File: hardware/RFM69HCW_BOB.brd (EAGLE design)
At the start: 27.9 x 20.3 mm, 13 parts, among them U1 RFM69HCW

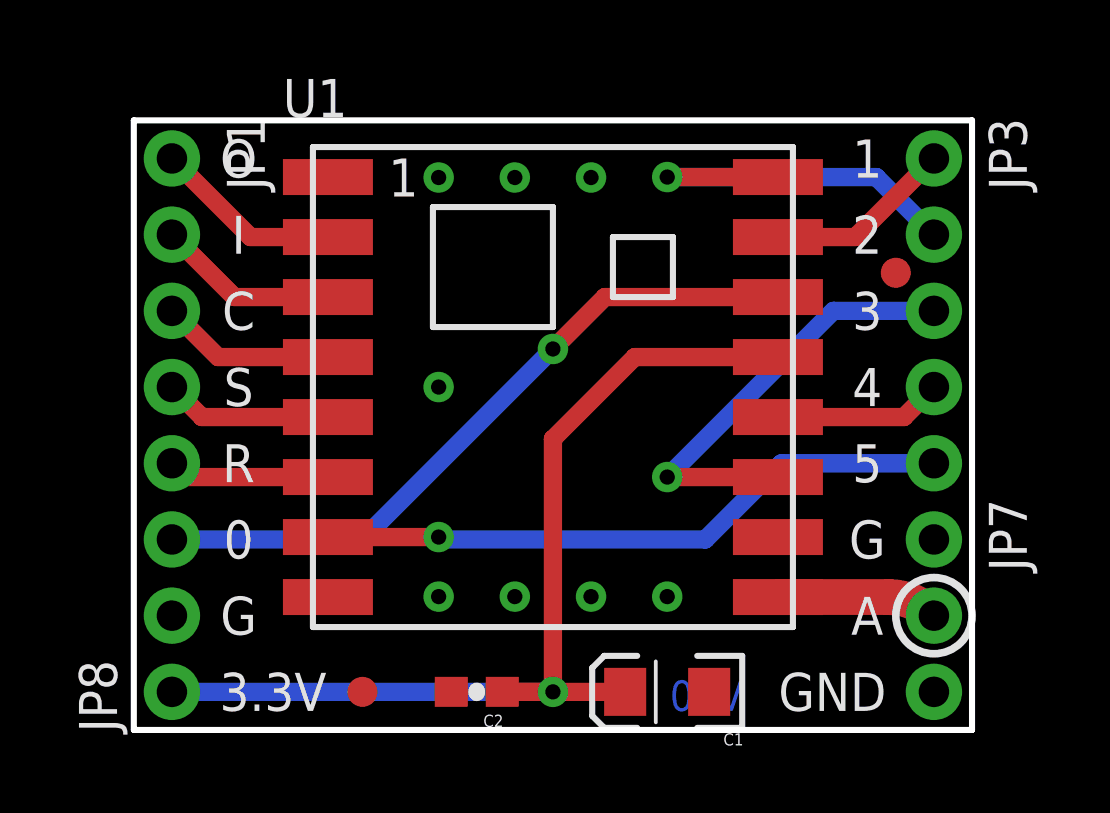
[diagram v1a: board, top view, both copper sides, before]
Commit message: Changed capacitor, removed C variant
Changed C1 to CAP-9824 (10uF ceramic for better transient response)
Removed RFM69C (low power) for future BOB
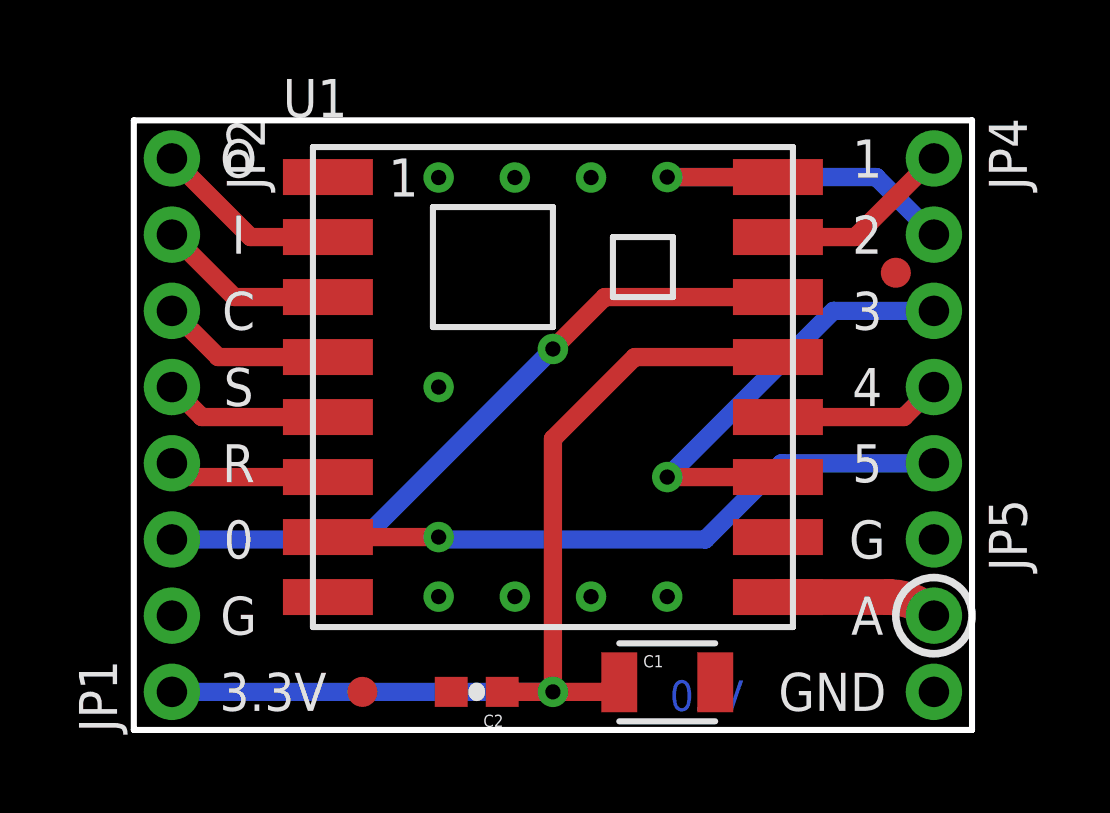
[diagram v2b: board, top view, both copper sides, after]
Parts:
- removed JP8: (no value), mike-temp:1X02_NO_SILK
- added JP4: (no value), mike-temp:1X05_ROUNDONLY_NOSILK
- C1: device SparkFun-Capacitors:EIA3216 -> SparkFun-Capacitors:1210
- JP1: device mike-temp:1X05_ROUNDONLY_NOSILK -> mike-temp:1X02_NO_SILK
- JP2: device mike-temp:1X01NS -> mike-temp:1X05_ROUNDONLY_NOSILK
- JP3: device mike-temp:1X05_ROUNDONLY_NOSILK -> mike-temp:1X01NS
- moved JP3 28.4 mm to (1.27, 6.35), turned to 0 degrees
- moved JP1 17.8 mm to (1.27, 1.27), turned to 90 degrees
- moved JP2 12.7 mm to (1.27, 19.1), turned to 270 degrees
- moved C1 0.32 mm to (17.8, 1.59), turned to 0 degrees
- renumbered JP7 to JP5
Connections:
- net 3.3V: now also C1.1, JP1.1; no longer C1.A, JP8.1
- net DIO0: now also JP3.1; no longer JP2.1
- net DIO1: now also JP4.1; no longer JP3.1
- net DIO2: now also JP4.2; no longer JP3.2
- net DIO3: now also JP4.3; no longer JP3.3
- net DIO4: now also JP4.4; no longer JP3.4
- net DIO5: now also JP4.5; no longer JP3.5
- net GND: now also C1.2, JP1.2; no longer C1.C, JP8.2
- net MISO: now also JP2.1; no longer JP1.1
- net MOSI: now also JP2.2; no longer JP1.2
- net NSS: now also JP2.4; no longer JP1.4
- net RESET: now also JP2.5; no longer JP1.5
- net SCK: now also JP2.3; no longer JP1.3
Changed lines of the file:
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@@
 <grid distance="0.05" unitdist="inch" unit="inch" style="lines" multiple="2" display="yes" altdistance="0.0125" altunitdist="inch" altunit="inch"/>
 <layers>
-<layer number="1" name="Top" color="4" fill="1" visible="yes" active="yes"/>
+<layer number="1" name="Top" color="4" fill="1" visible="no" active="yes"/>
 <layer number="2" name="Route2" color="1" fill="3" visible="no" active="no"/>
 <layer number="3" name="Route3" color="4" fill="3" visible="no" active="no"/>
@@
 <layer number="19" name="Unrouted" color="6" fill="1" visible="yes" active="yes"/>
 <layer number="20" name="Dimension" color="15" fill="1" visible="yes" active="yes"/>
-<layer number="21" name="tPlace" color="7" fill="1" visible="yes" active="yes"/>
-<layer number="22" name="bPlace" color="7" fill="1" visible="no" active="yes"/>
-<layer number="23" name="tOrigins" color="15" fill="1" visible="yes" active="yes"/>
-<layer number="24" name="bOrigins" color="15" fill="1" visible="no" active="yes"/>
+<layer number="21" name="tPlace" color="7" fill="1" visible="no" active="yes"/>
+<layer number="22" name="bPlace" color="7" fill="1" visible="yes" active="yes"/>
+<layer number="23" name="tOrigins" color="15" fill="1" visible="no" active="yes"/>
+<layer number="24" name="bOrigins" color="15" fill="1" visible="yes" active="yes"/>
 <layer number="25" name="tNames" color="7" fill="1" visible="no" active="yes"/>
 <layer number="26" name="bNames" color="7" fill="1" visible="no" active="yes"/>
 <layer number="27" name="tValues" color="7" fill="1" visible="no" active="yes"/>
 <layer number="28" name="bValues" color="7" fill="1" visible="no" active="yes"/>
-<layer number="29" name="tStop" color="7" fill="3" visible="yes" active="yes"/>
-<layer number="30" name="bStop" color="7" fill="6" visible="no" active="yes"/>
-<layer number="31" name="tCream" color="7" fill="4" visible="yes" active="yes"/>
+<layer number="29" name="tStop" color="7" fill="3" visible="no" active="yes"/>
+<layer number="30" name="bStop" color="7" fill="6" visible="yes" active="yes"/>
+<layer number="31" name="tCream" color="7" fill="4" visible="no" active="yes"/>
 <layer number="32" name="bCream" color="7" fill="5" visible="no" active="yes"/>
 <layer number="33" name="tFinish" color="6" fill="3" visible="no" active="yes"/>
@@
 <text x="19.05" y="2.54" size="1.27" layer="22" ratio="15" rot="MR0">(6.5" 164mm)</text>
 <text x="19.05" y="6.35" size="1.27" layer="22" ratio="15" rot="MR0">(3.1" 78mm)</text>
+<rectangle x1="19.05" y1="0.635" x2="20.32" y2="1.905" layer="22"/>
+<rectangle x1="11.43" y1="0.635" x2="12.7" y2="1.905" layer="22"/>
 </plain>
 <attributes>
@@
 <attribute name="PROD_ID" value="CAP-00810" x="-3.81" y="38.1" size="1.778" layer="27" rot="R180" display="off"/>
 </element>
-<element name="C1" library="SparkFun-Capacitors" package="EIA3216" value="10uF" x="17.78" y="1.27" rot="R180">
-<attribute name="PROD_ID" value="CAP-00811" x="-27.94" y="31.75" size="1.778" layer="27" rot="R180" display="off"/>
-</element>
 <element name="LOGO1" library="SparkFun-Aesthetics" package="SFE_LOGO_NAME_.1" value="SFE_LOGO_NAME.1_INCH" x="20.0025" y="14.2875" rot="MR0"/>
 <element name="LOGO2" library="SparkFun-Aesthetics" package="OSHW-LOGO-S" value="OSHW-LOGOS" x="13.97" y="11.43" rot="MR0"/>
-<element name="JP7" library="mike-temp" package="1X03_ROUND_ONLY_NO_SILK" value="ANTENNA" x="26.67" y="6.35" rot="R270"/>
-<element name="JP8" library="mike-temp" package="1X02_NO_SILK" value="" x="1.27" y="1.27" rot="R90"/>
-<element name="JP1" library="mike-temp" package="1X05_ROUNDONLY_NOSILK" value="" x="1.27" y="19.05" rot="R270"/>
-<element name="JP2" library="mike-temp" package="1X01NS" value="" x="1.27" y="6.35"/>
-<element name="JP3" library="mike-temp" package="1X05_ROUNDONLY_NOSILK" value="" x="26.67" y="19.05" rot="R270"/>
+<element name="JP5" library="mike-temp" package="1X03_ROUND_ONLY_NO_SILK" value="ANTENNA" x="26.67" y="6.35" rot="R270"/>
+<element name="JP1" library="mike-temp" package="1X02_NO_SILK" value="" x="1.27" y="1.27" rot="R90"/>
+<element name="JP2" library="mike-temp" package="1X05_ROUNDONLY_NOSILK" value="" x="1.27" y="19.05" rot="R270"/>
+<element name="JP3" library="mike-temp" package="1X01NS" value="" x="1.27" y="6.35"/>
+<element name="JP4" library="mike-temp" package="1X05_ROUNDONLY_NOSILK" value="" x="26.67" y="19.05" rot="R270"/>
 <element name="FID1" library="SparkFun-Aesthetics" package="FIDUCIAL-1X2" value="FIDUCIAL1X2" x="7.62" y="1.27"/>
 <element name="FID2" library="SparkFun-Aesthetics" package="FIDUCIAL-1X2" value="FIDUCIAL1X2" x="25.4" y="15.24"/>
+<element name="C1" library="SparkFun-Capacitors" package="1210" value="10uF" x="17.78" y="1.5875">
+<attribute name="PROD_ID" value="CAP-09824" x="17.78" y="1.5875" size="1.778" layer="27" display="off"/>
+</element>
 </elements>
 <signals>
@@
 <contactref element="U1" pad="8"/>
 <contactref element="U1" pad="1"/>
-<contactref element="C1" pad="C"/>
 <contactref element="C2" pad="2"/>
 <polygon width="0.2032" layer="16" isolate="0.3048">
@@
 <via x="17.78" y="4.445" extent="1-16" drill="0.508"/>
 <via x="10.16" y="4.445" extent="1-16" drill="0.508"/>
-<contactref element="JP7" pad="1"/>
-<contactref element="JP7" pad="3"/>
+<contactref element="JP5" pad="1"/>
+<contactref element="JP5" pad="3"/>
 <contactref element="U1" pad="10"/>
 <via x="12.7" y="4.445" extent="1-16" drill="0.508"/>
 <via x="15.24" y="4.445" extent="1-16" drill="0.508"/>
-<contactref element="JP8" pad="2"/>
+<contactref element="JP1" pad="2"/>
 <via x="12.7" y="18.415" extent="1-16" drill="0.508"/>
 <via x="15.24" y="18.415" extent="1-16" drill="0.508"/>
 <via x="10.16" y="18.415" extent="1-16" drill="0.508"/>
 <via x="10.16" y="11.43" extent="1-16" drill="0.508"/>
+<contactref element="C1" pad="2"/>
 </signal>
 <signal name="3.3V">
 <contactref element="C2" pad="1"/>
-<contactref element="C1" pad="A"/>
 <wire x1="16.699759375" y1="12.43" x2="13.97" y2="9.700240625" width="0.6096" layer="1"/>
 <wire x1="13.97" y1="9.700240625" x2="13.97" y2="1.27" width="0.6096" layer="1"/>
 <via x="13.97" y="1.27" extent="1-16" drill="0.508"/>
-<wire x1="13.97" y1="1.27" x2="16.38" y2="1.27" width="0.6096" layer="1"/>
 <wire x1="13.97" y1="1.27" x2="12.28" y2="1.27" width="0.6096" layer="1"/>
-<contactref element="JP8" pad="1"/>
+<contactref element="JP1" pad="1"/>
 <contactref element="U1" pad="13"/>
 <wire x1="16.699759375" y1="12.43" x2="21.47" y2="12.43" width="0.6096" layer="1"/>
 <wire x1="1.27" y1="1.27" x2="13.97" y2="1.27" width="0.6096" layer="16"/>
+<contactref element="C1" pad="1"/>
+<wire x1="13.97" y1="1.27" x2="16.18" y2="1.27" width="0.6096" layer="1"/>
+<wire x1="16.18" y1="1.27" x2="16.18" y2="1.5875" width="0.6096" layer="1"/>
 </signal>
 <signal name="DIO0">
 <contactref element="U1" pad="14"/>
-<contactref element="JP2" pad="1"/>
+<contactref element="JP3" pad="1"/>
 <wire x1="21.47" y1="14.43" x2="15.7" y2="14.43" width="0.6096" layer="1"/>
 <wire x1="15.7" y1="14.43" x2="13.97" y2="12.7" width="0.6096" layer="1"/>
@@
 <signal name="DIO1">
 <contactref element="U1" pad="15"/>
-<contactref element="JP3" pad="1"/>
+<contactref element="JP4" pad="1"/>
 <wire x1="21.47" y1="16.43" x2="24.05" y2="16.43" width="0.6096" layer="1"/>
 <wire x1="24.05" y1="16.43" x2="26.67" y2="19.05" width="0.6096" layer="1"/>
@@
 <signal name="DIO2">
 <contactref element="U1" pad="16"/>
-<contactref element="JP3" pad="2"/>
+<contactref element="JP4" pad="2"/>
 <wire x1="21.47" y1="18.43" x2="17.78" y2="18.43" width="0.6096" layer="1"/>
 <via x="17.78" y="18.43" extent="1-16" drill="0.508"/>
@@
 <signal name="DIO3">
 <contactref element="U1" pad="11"/>
-<contactref element="JP3" pad="3"/>
+<contactref element="JP4" pad="3"/>
 <wire x1="21.47" y1="8.43" x2="17.78" y2="8.43" width="0.6096" layer="1"/>
 <via x="17.78" y="8.43" extent="1-16" drill="0.508"/>
@@
 <contactref element="U1" pad="2"/>
 <wire x1="6.47" y1="16.43" x2="3.89" y2="16.43" width="0.6096" layer="1"/>
-<contactref element="JP1" pad="1"/>
+<contactref element="JP2" pad="1"/>
 <wire x1="3.89" y1="16.43" x2="1.27" y2="19.05" width="0.6096" layer="1"/>
 </signal>
@@
 <contactref element="U1" pad="3"/>
 <wire x1="6.47" y1="14.43" x2="3.35" y2="14.43" width="0.6096" layer="1"/>
-<contactref element="JP1" pad="2"/>
+<contactref element="JP2" pad="2"/>
 <wire x1="3.35" y1="14.43" x2="1.27" y2="16.51" width="0.6096" layer="1"/>
 </signal>
@@
 <contactref element="U1" pad="4"/>
 <wire x1="6.47" y1="12.43" x2="2.81" y2="12.43" width="0.6096" layer="1"/>
-<contactref element="JP1" pad="3"/>
+<contactref element="JP2" pad="3"/>
 <wire x1="2.81" y1="12.43" x2="1.27" y2="13.97" width="0.6096" layer="1"/>
 </signal>
@@
 <contactref element="U1" pad="5"/>
 <wire x1="6.47" y1="10.43" x2="2.27" y2="10.43" width="0.6096" layer="1"/>
-<contactref element="JP1" pad="4"/>
+<contactref element="JP2" pad="4"/>
 <wire x1="2.27" y1="10.43" x2="1.27" y2="11.43" width="0.6096" layer="1"/>
 </signal>
@@
 <contactref element="U1" pad="6"/>
 <wire x1="6.47" y1="8.43" x2="1.73" y2="8.43" width="0.6096" layer="1"/>
-<contactref element="JP1" pad="5"/>
+<contactref element="JP2" pad="5"/>
 <wire x1="1.73" y1="8.43" x2="1.27" y2="8.89" width="0.6096" layer="1"/>
 </signal>
 <signal name="ANT">
-<contactref element="JP7" pad="2"/>
+<contactref element="JP5" pad="2"/>
 <contactref element="U1" pad="9"/>
 <wire x1="21.47" y1="4.43" x2="25.1731875" y2="4.43" width="1.1938" layer="1"/>
@@
 <signal name="DIO5">
 <contactref element="U1" pad="7"/>
-<contactref element="JP3" pad="5"/>
+<contactref element="JP4" pad="5"/>
 <wire x1="6.47" y1="6.43" x2="10.16" y2="6.43" width="0.6096" layer="1"/>
 <via x="10.16" y="6.43" extent="1-16" drill="0.508"/>
@@
 <signal name="DIO4">
 <contactref element="U1" pad="12"/>
-<contactref element="JP3" pad="4"/>
+<contactref element="JP4" pad="4"/>
 <wire x1="21.47" y1="10.43" x2="25.67" y2="10.43" width="0.6096" layer="1"/>
 <wire x1="25.67" y1="10.43" x2="26.67" y2="11.43" width="0.6096" layer="1"/>
